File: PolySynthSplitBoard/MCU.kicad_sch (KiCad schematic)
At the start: 79 parts, among them J401 PWR, J402 DATA, J403 SWD Header, J404 MIDI_In, J405 Micro_SD_Card_Det2, J406 MIDI_Out, J407 MIDI_Thru, SW401 RST, SW402 BOOT, U401 STM32F411RETx, U402 74HC595, U403 74HC595, U404 74HC04, U405 6N138, Y401 16MHz, Y402 32.768kHZ

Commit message: lower board
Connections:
- net V1_CLK1: now also R434.2; no longer R424.2
- net V1_CLK2: now also R433.2; no longer R425.2
- net V2_CLK1: now also R435.2; no longer R426.2
- net V2_CLK2: now also R432.2; no longer R427.2
- net V3_CLK1: now also R431.2; no longer R428.2
- net V3_CLK2: now also R430.2; no longer R429.2
- net V4_CLK1: now also R429.2; no longer R430.2
- net V4_CLK2: now also R428.2; no longer R431.2
- net V5_CLK1: now also R427.2; no longer R432.2
- net V5_CLK2: now also R426.2; no longer R435.2
- net V6_CLK1: now also R425.2; no longer R433.2
- net V6_CLK2: now also R424.2; no longer R434.2

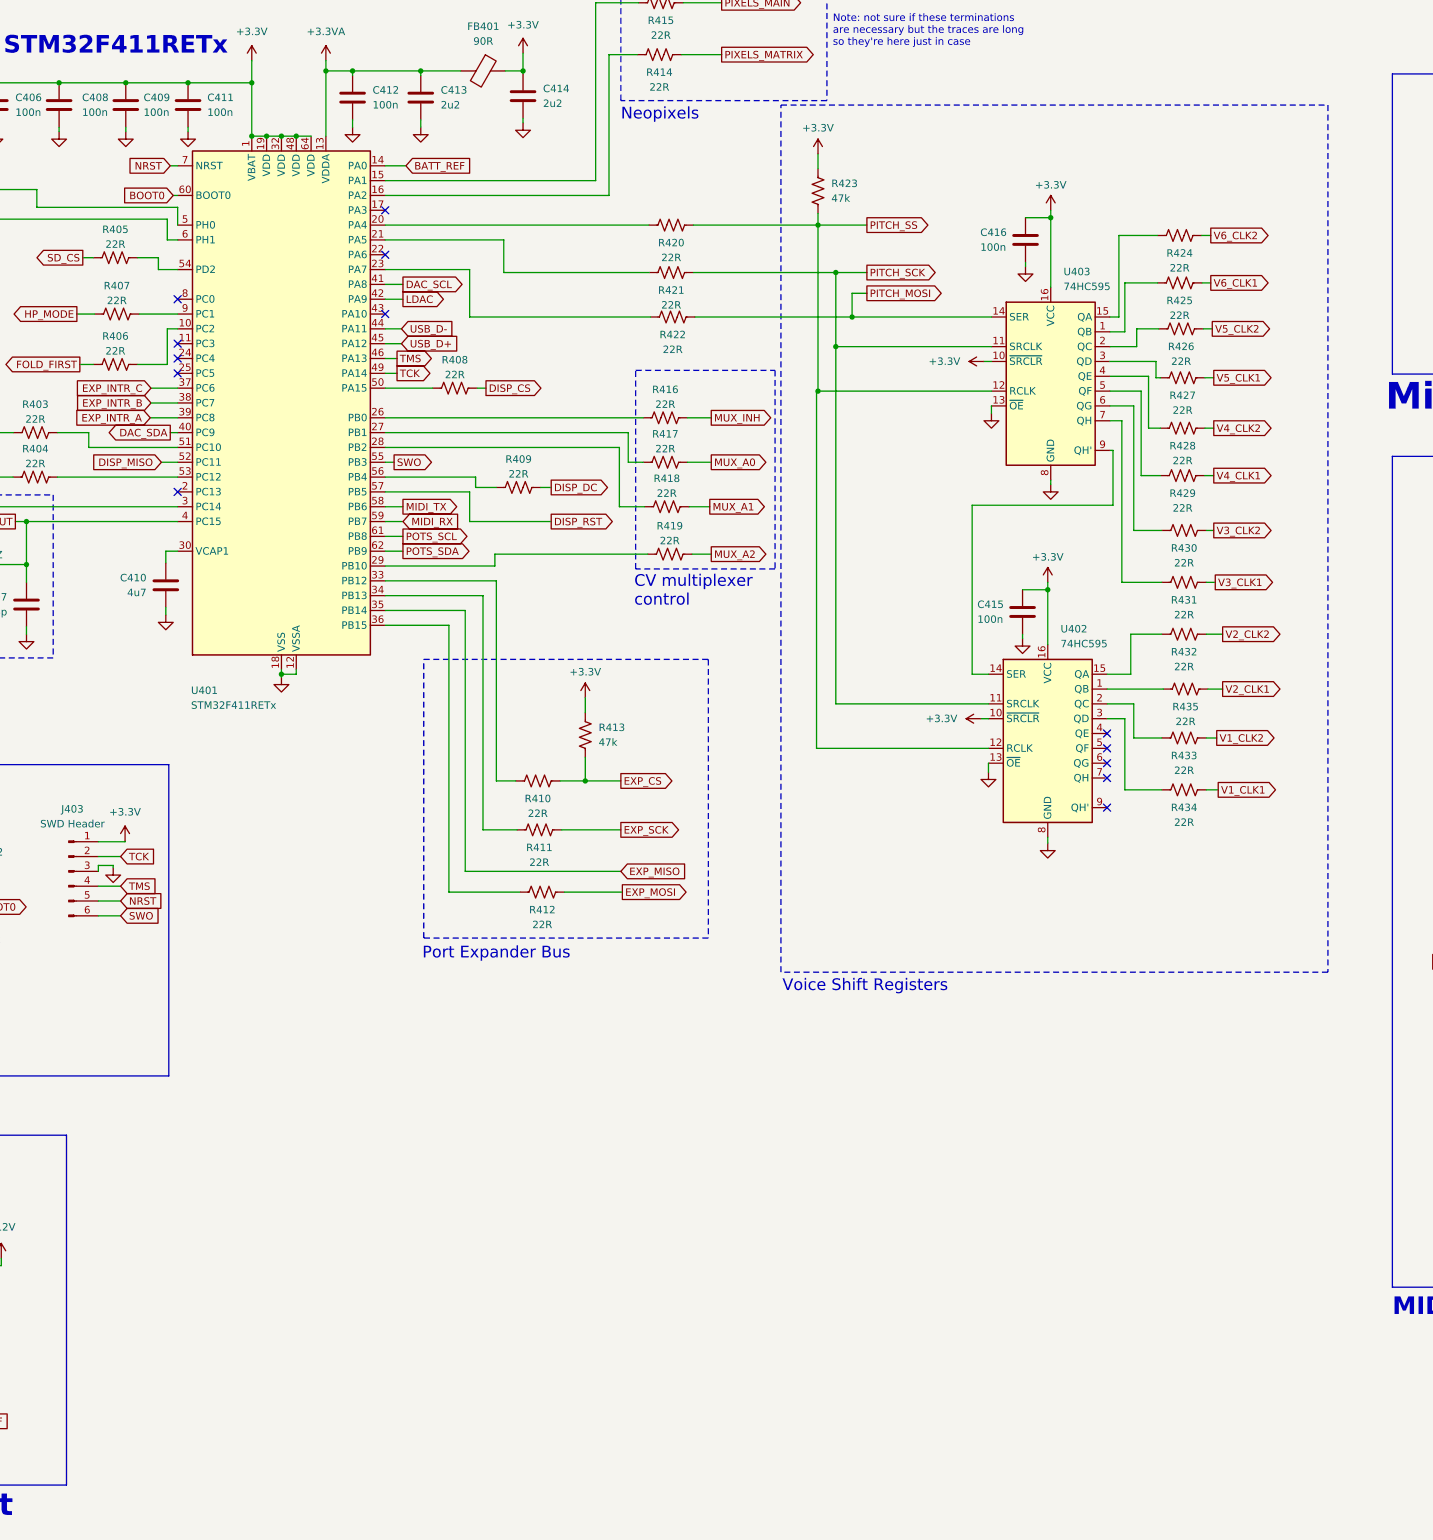
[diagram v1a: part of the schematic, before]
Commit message: removed copper pour
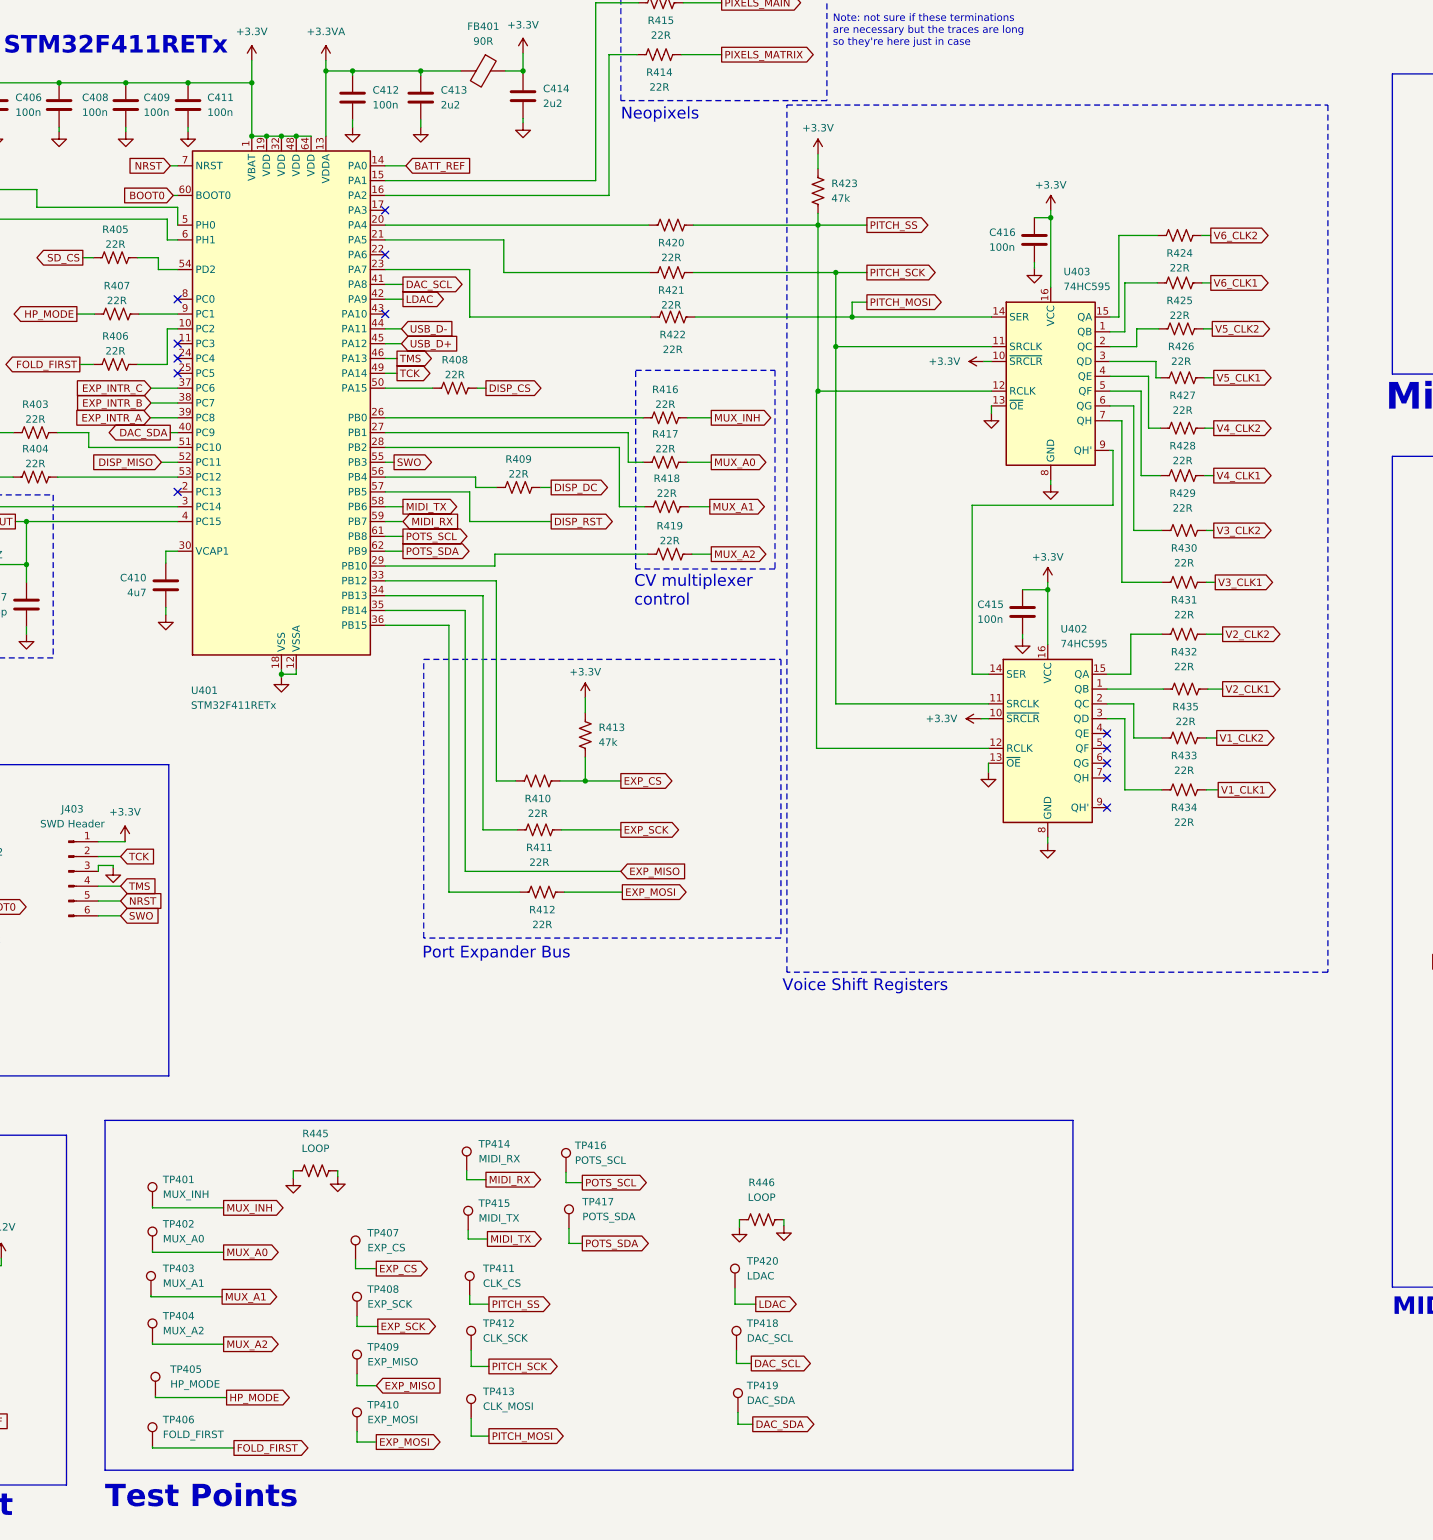
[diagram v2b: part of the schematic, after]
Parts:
- added R445, R446: LOOP, Resistor_THT:R_Axial_DIN0204_L3.6mm_D1.6mm_P5.08mm_Horizontal, symbol Device:R_US
- added TP401: MUX_INH, TestPoint:TestPoint_THTPad_D1.5mm_Drill0.7mm_VAL, symbol Connector:TestPoint
- added TP402: MUX_A0, TestPoint:TestPoint_THTPad_D1.5mm_Drill0.7mm_VAL, symbol Connector:TestPoint
- added TP403: MUX_A1, TestPoint:TestPoint_THTPad_D1.5mm_Drill0.7mm_VAL, symbol Connector:TestPoint
- added TP404: MUX_A2, TestPoint:TestPoint_THTPad_D1.5mm_Drill0.7mm_VAL, symbol Connector:TestPoint
- added TP405: HP_MODE, TestPoint:TestPoint_THTPad_D1.5mm_Drill0.7mm_VAL, symbol Connector:TestPoint
- added TP406: FOLD_FIRST, TestPoint:TestPoint_THTPad_D1.5mm_Drill0.7mm_VAL, symbol Connector:TestPoint
- added TP407: EXP_CS, TestPoint:TestPoint_THTPad_D1.0mm_Drill0.5mm_VAL, symbol Connector:TestPoint
- added TP408: EXP_SCK, TestPoint:TestPoint_THTPad_D1.0mm_Drill0.5mm_VAL, symbol Connector:TestPoint
- added TP409: EXP_MISO, TestPoint:TestPoint_THTPad_D1.0mm_Drill0.5mm_VAL, symbol Connector:TestPoint
- added TP410: EXP_MOSI, TestPoint:TestPoint_THTPad_D1.0mm_Drill0.5mm_VAL, symbol Connector:TestPoint
- added TP411: CLK_CS, TestPoint:TestPoint_THTPad_D1.0mm_Drill0.5mm_VAL, symbol Connector:TestPoint
- added TP412: CLK_SCK, TestPoint:TestPoint_THTPad_D1.0mm_Drill0.5mm_VAL, symbol Connector:TestPoint
- added TP413: CLK_MOSI, TestPoint:TestPoint_THTPad_D1.0mm_Drill0.5mm_VAL, symbol Connector:TestPoint
- added TP414: MIDI_RX, TestPoint:TestPoint_THTPad_D1.0mm_Drill0.5mm_VAL, symbol Connector:TestPoint
- added TP415: MIDI_TX, TestPoint:TestPoint_THTPad_D1.0mm_Drill0.5mm_VAL, symbol Connector:TestPoint
- added TP416: POTS_SCL, TestPoint:TestPoint_THTPad_D1.0mm_Drill0.5mm_VAL, symbol Connector:TestPoint
- added TP417: POTS_SDA, TestPoint:TestPoint_THTPad_D1.0mm_Drill0.5mm_VAL, symbol Connector:TestPoint
- added TP418: DAC_SCL, TestPoint:TestPoint_THTPad_D1.0mm_Drill0.5mm_VAL, symbol Connector:TestPoint
- added TP419: DAC_SDA, TestPoint:TestPoint_THTPad_D1.0mm_Drill0.5mm_VAL, symbol Connector:TestPoint
- added TP420: LDAC, TestPoint:TestPoint_THTPad_D1.0mm_Drill0.5mm_VAL, symbol Connector:TestPoint
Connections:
- net DAC_SCL: now also TP418.1
- net DAC_SDA: now also TP419.1
- net EXP_CS: now also TP407.1
- net EXP_MISO: now also TP409.1
- net EXP_MOSI: now also TP410.1
- net EXP_SCK: now also TP408.1
- net FOLD_FIRST: now also TP406.1
- net GND: now also R445.1, R445.2, R446.1, R446.2
- net HP_MODE: now also TP405.1
- net LDAC: now also TP420.1
- net MIDI_RX: now also TP414.1
- net MIDI_TX: now also TP415.1
- net MUX_A0: now also TP402.1
- net MUX_A1: now also TP403.1
- net MUX_A2: now also TP404.1
- net MUX_INH: now also TP401.1
- net PITCH_MOSI: now also TP413.1
- net PITCH_SCK: now also TP412.1
- net PITCH_SS: now also TP411.1
- net POTS_SCL: now also TP416.1
- net POTS_SDA: now also TP417.1
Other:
- note added: "Test Points"
- moved on the sheet: C416
